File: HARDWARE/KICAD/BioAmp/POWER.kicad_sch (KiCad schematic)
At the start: 16 parts, among them U2 MP1484, U3 AMS1117-3.3

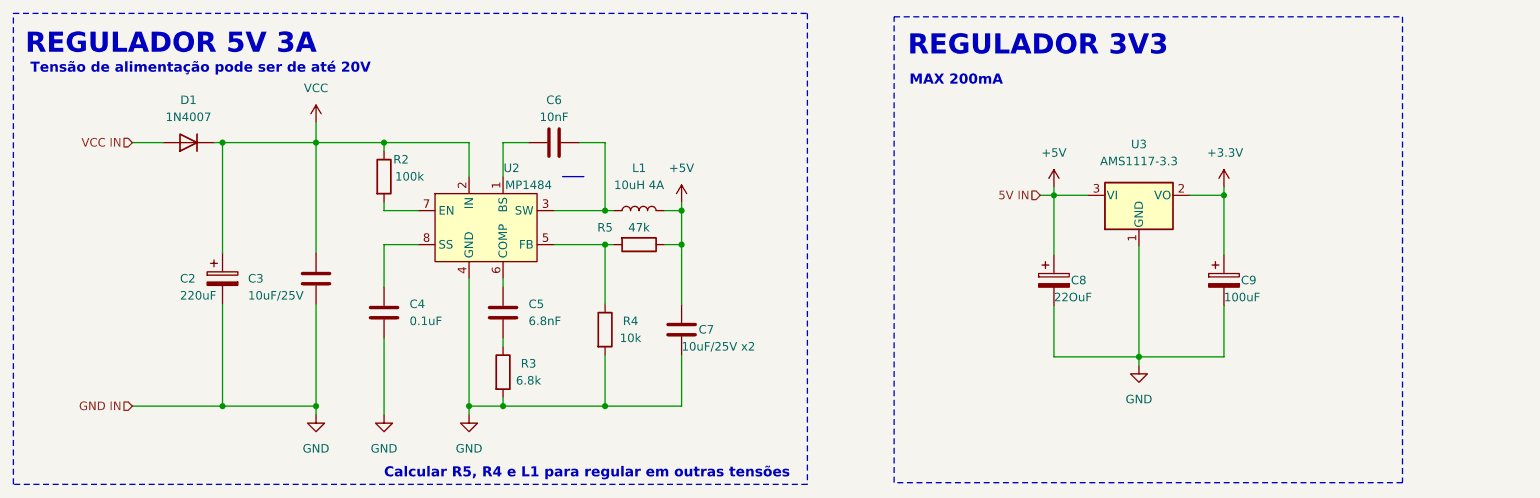
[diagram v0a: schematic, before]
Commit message: Corrigido circuito AFE (Analog Front End); adição dos ports necessários na folha principal; transferência do LED de indicação de energia para folha de fontes; adição da sugestão para novo ADC.
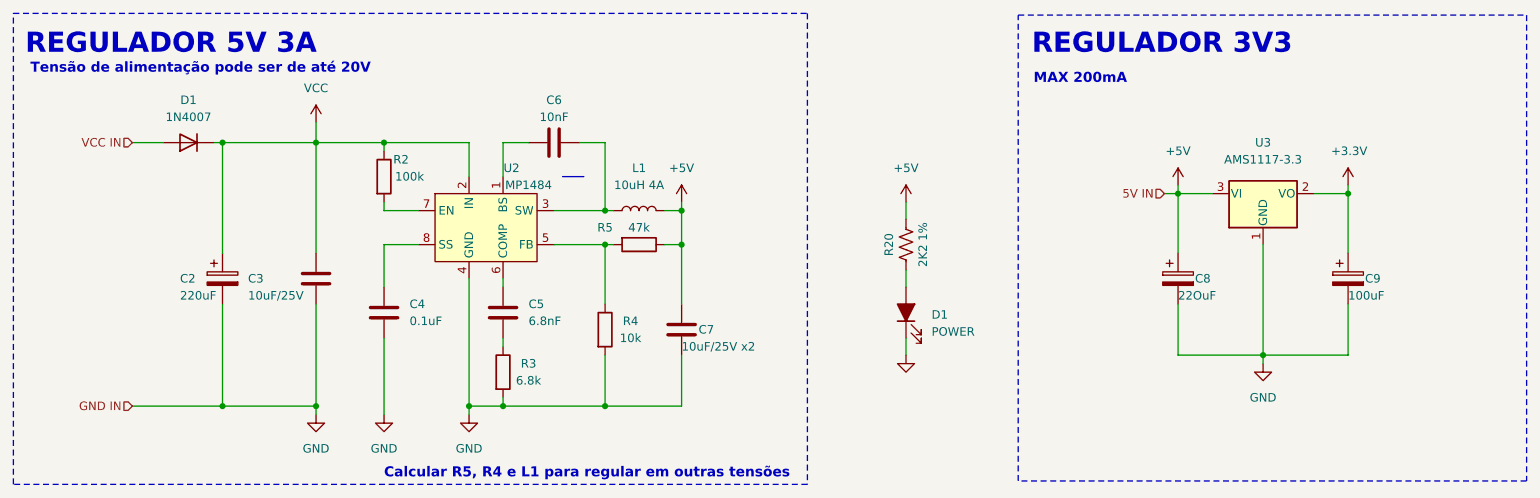
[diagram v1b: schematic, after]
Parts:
- added D1: POWER, symbol Device:LED_Filled
- added R20: 2K2 1%, symbol Device:R_US
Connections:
- net +5V: now also R20.2
- net GND: now also D1.1 (K)
- new net: D1.2 (A), R20.1
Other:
- moved on the sheet: C8, C9, U3
